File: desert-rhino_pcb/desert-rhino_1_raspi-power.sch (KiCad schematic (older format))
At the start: 6 parts

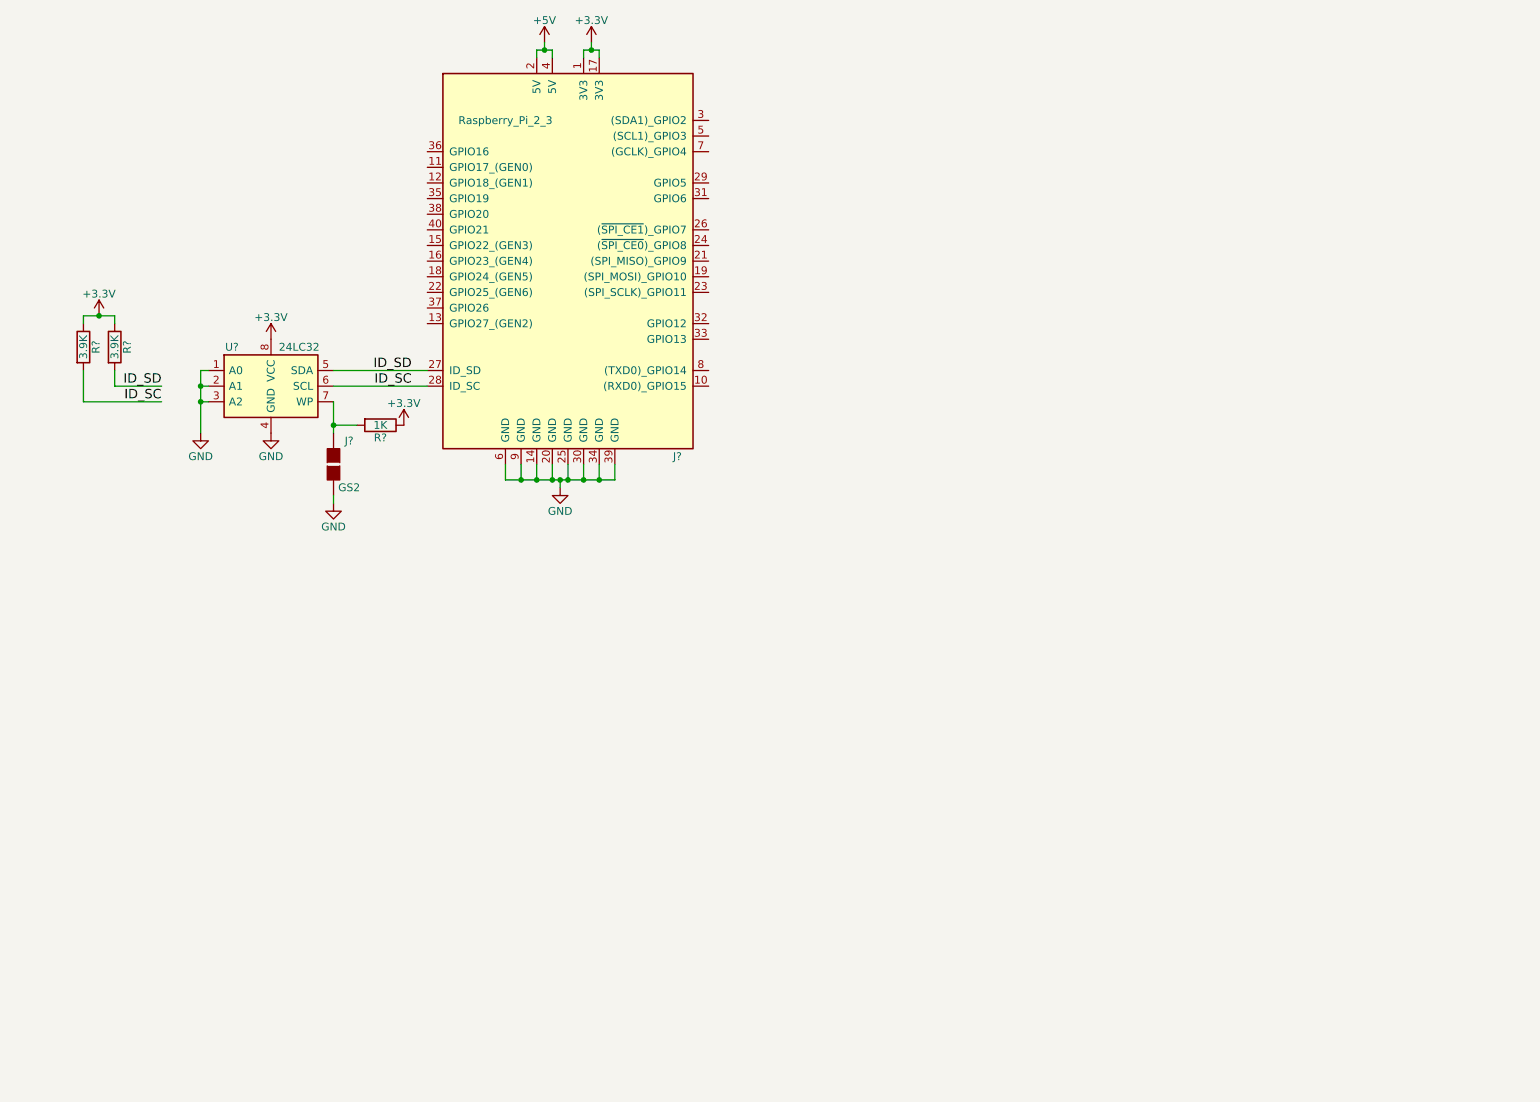
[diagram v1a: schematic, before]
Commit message: Finished most of schem. Still need ina230
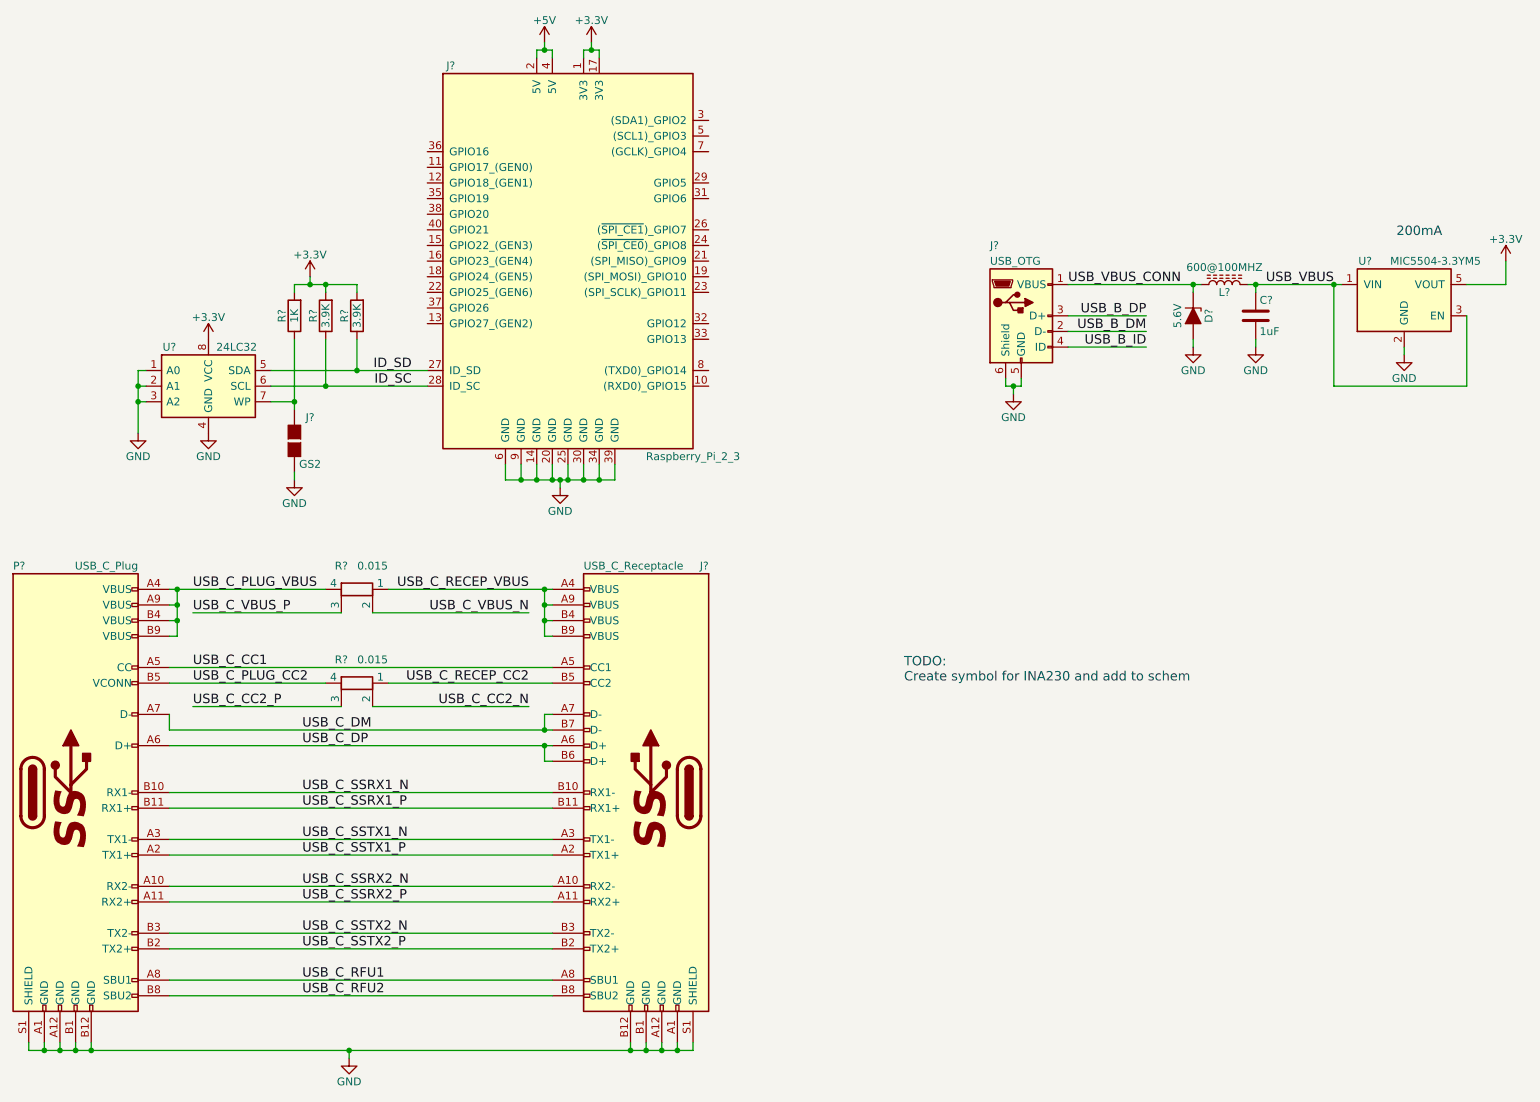
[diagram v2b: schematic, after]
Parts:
- removed R?: 3.9K, symbol R
- added C?: 1uF, symbol C
- added D?: 5.6V, symbol D_Zener_ALT
- added J?: USB_OTG, symbol USB_OTG
- added J?: USB_C_Receptacle, symbol USB_C_Receptacle
- added L?: 600@100MHZ, symbol L_Core_Ferrite
- added P?: USB_C_Plug, symbol USB_C_Plug
- added R?: 3.9K, Resistors_SMD:R_0603_HandSoldering, symbol R
- added R? (x2): 0.015, symbol R_Shunt
- added U?: MIC5504-3.3YM5, TO_SOT_Packages_SMD:SOT-23-5, symbol MIC5504-3.3YM5
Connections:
- net +3V3: now also R?.2, R?.2, R?.2, U?.5 (VOUT); no longer R?.1, R?.1
- net GND: now also C?.2, D?.2 (A), J?.5 (GND), J?.6 (Shield), J?.A1 (GND), J?.A12 (GND), J?.B1 (GND), J?.B12 (GND), J?.S1 (SHIELD), P?.A1 (GND), P?.A12 (GND), P?.B1 (GND), P?.B12 (GND), P?.S1 (SHIELD), U?.2 (GND)
- net ID_SC: now also R?.1; no longer R?.2
- net ID_SD: now also R?.1
- net at J?.1 (G1), U?.7 (WP): now also R?.1; no longer R?.2
- new net USB_B_DM: J?.2 (D-)
- new net USB_B_DP: J?.3 (D+)
- new net USB_B_ID: J?.4 (ID)
- new net USB_C_CC1: J?.A5 (CC1), P?.A5 (CC)
- new net USB_C_CC2_N: R?.2
- new net USB_C_CC2_P: R?.3
- new net USB_C_DM: J?.A7 (D-), J?.B7 (D-), P?.A7 (D-)
- new net USB_C_DP: J?.A6 (D+), J?.B6 (D+), P?.A6 (D+)
- new net USB_C_PLUG_CC2: P?.B5 (VCONN), R?.4
- new net USB_C_PLUG_VBUS: P?.A4 (VBUS), P?.A9 (VBUS), P?.B4 (VBUS), P?.B9 (VBUS), R?.4
- new net USB_C_RECEP_CC2: J?.B5 (CC2), R?.1
- new net USB_C_RECEP_VBUS: J?.A4 (VBUS), J?.A9 (VBUS), J?.B4 (VBUS), J?.B9 (VBUS), R?.1
- new net USB_C_RFU1: J?.A8 (SBU1), P?.A8 (SBU1)
- new net USB_C_RFU2: J?.B8 (SBU2), P?.B8 (SBU2)
- new net USB_C_SSRX1_N: J?.B10 (RX1-), P?.B10 (RX1-)
- new net USB_C_SSRX1_P: J?.B11 (RX1+), P?.B11 (RX1+)
- new net USB_C_SSRX2_N: J?.A10 (RX2-), P?.A10 (RX2-)
- new net USB_C_SSRX2_P: J?.A11 (RX2+), P?.A11 (RX2+)
- new net USB_C_SSTX1_N: J?.A3 (TX1-), P?.A3 (TX1-)
- new net USB_C_SSTX1_P: J?.A2 (TX1+), P?.A2 (TX1+)
- new net USB_C_SSTX2_N: J?.B3 (TX2-), P?.B3 (TX2-)
- new net USB_C_SSTX2_P: J?.B2 (TX2+), P?.B2 (TX2+)
- new net USB_C_VBUS_N: R?.2
- new net USB_C_VBUS_P: R?.3
- new net USB_VBUS: C?.1, L?.2, U?.1 (VIN), U?.3 (EN)
- new net USB_VBUS_CONN: D?.1 (K), J?.1 (VBUS), L?.1
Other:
- note added: "200mA"
- note added: "TODO:\nCreate symbol for INA230 and add to schem"
- moved on the sheet: J?, R?, U?
